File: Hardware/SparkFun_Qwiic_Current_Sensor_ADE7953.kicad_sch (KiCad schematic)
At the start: 34 parts, among them IC1 ADE7953ACPZ, J1 Qwiic_RA, J2 Qwiic_RA, J3 Conn_01x06, J4 Conn_01x04, J5 3.5mm TRRS, Y1 Resonator

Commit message: Updated PCB and Schematic
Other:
- note added: "Be sure to change these shunt resistor values!"
- note removed: "Be sure to change these shunt capacitor values!"
- moved on the sheet: R4, R5

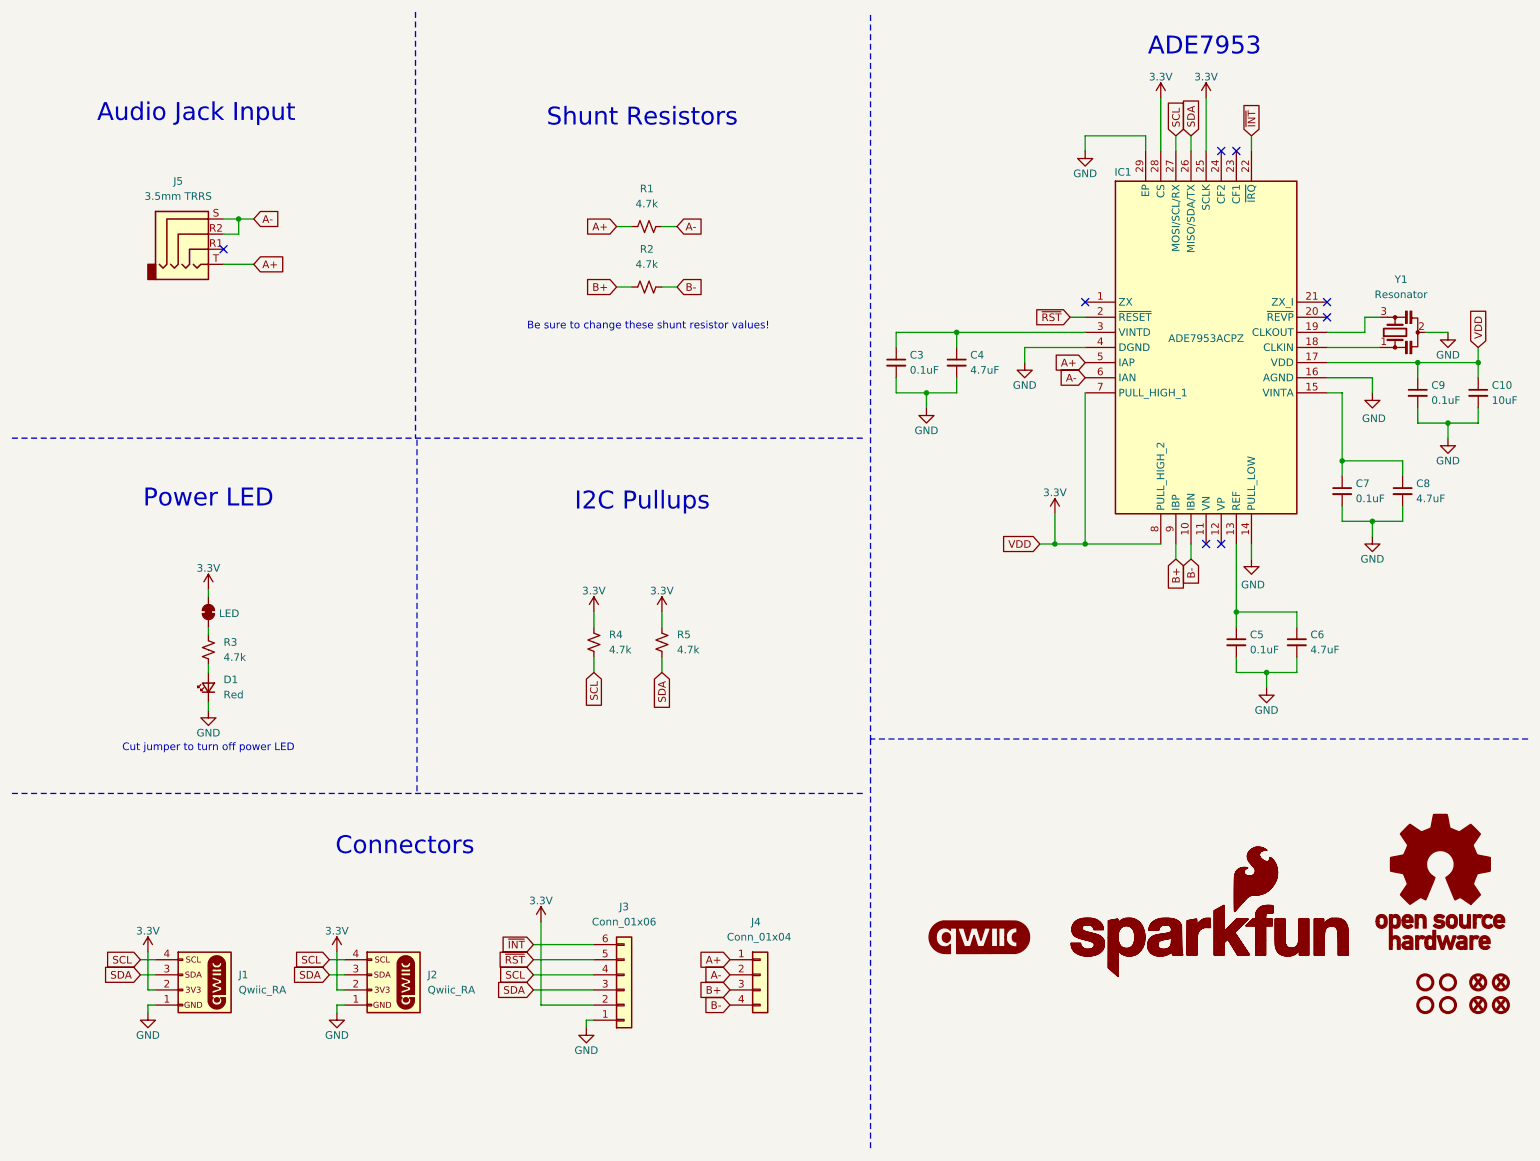
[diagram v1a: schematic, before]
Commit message: Updated IC Schematic Symbols
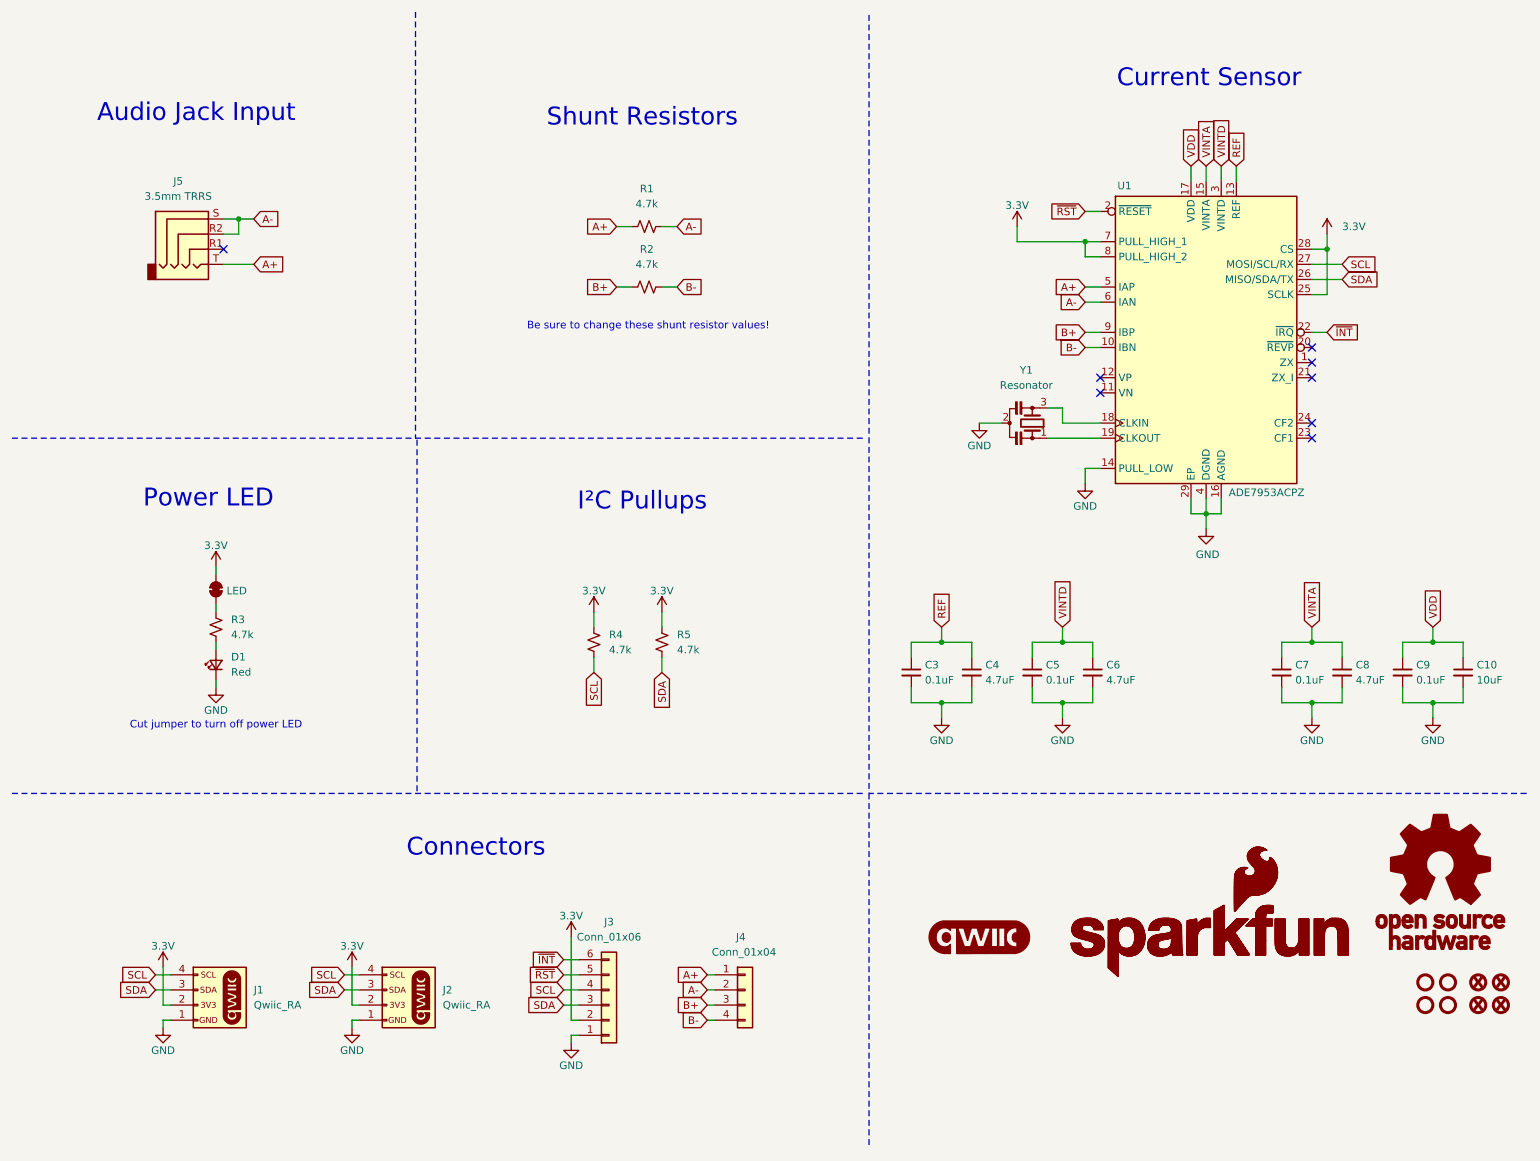
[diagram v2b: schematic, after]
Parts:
- renumbered IC1 to U1
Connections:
- net 3.3V: no longer C10.1, C9.1, U1.17 (VDD)
- net VINTD: now reaches C5.1, C6.1
- net VINTD: now also U1.3 (VINTD); no longer U1.13 (REF)
- net at Y1.1: now also U1.19 (CLKOUT); no longer U1.18 (CLKIN)
- net at Y1.3: now also U1.18 (CLKIN); no longer U1.19 (CLKOUT)
- net REF: now reaches C3.1, C4.1
- net REF: now also U1.13 (REF); no longer U1.3 (VINTD)
- net VINTA: now reaches C7.1, C8.1, U1.15 (VINTA)
- new net VDD: C10.1, C9.1, U1.17 (VDD)
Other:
- note added: "Current Sensor"
- note added: "I²C Pullups"
- note removed: "ADE7953"
- note removed: "I2C Pullups"
- title: SparkFun Qwiic 5V Boost AP3012K -> SparkFun Qwiic Current Sensor ADE7953
- moved on the sheet: C10, C3, C4, C5, C6, C7, C8, C9, D1, J1, J2, J3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

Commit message: Updated PCB Layout
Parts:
- removed C10: 10uF, SparkFun-Capacitor:C_0603_1608Metric, symbol SparkFun-Capacitor:10uF_0603_10V_20%
- removed C3, C5, C7, C9: 0.1uF, SparkFun-Capacitor:C_0603_1608Metric, symbol SparkFun-Capacitor:0.1uF_0603_25V_20%
- removed C4, C6, C8: 4.7uF, SparkFun-Capacitor:C_0603_1608Metric, symbol SparkFun-Capacitor:4.7uF_0603_35V_20%
- removed J4: Conn_01x04, SparkFun-Connector:1x04_P2.54mm, symbol SparkFun-Connector:Conn_01x04_P2.54mm
- added C1, C2, C3, C4: 1.0uF, SparkFun-Capacitor:C_0402_1005Metric, symbol SparkFun-Capacitor:1.0uF_0402_16V_10%
- added J4, J6: Conn_01x02, SparkFun-Connector:1x02_P2.54mm, symbol SparkFun-Connector:Conn_01x02_P2.54mm
- added JP2: ~, SparkFun-Jumper:Jumper_3_NC-2_Trace, symbol SparkFun-Jumper:SolderJumper_3_Bridged123
- R1, R2: value 4.7k -> 100; footprint SparkFun-Resistor:R_0603_1608Metric -> SparkFun-Resistor:R_0402_1005Metric; symbol SparkFun-Resistor:4.7k_0603 -> SparkFun-Resistor:100_0402; PROD_ID RES-07857 -> RES-25568
- R4, R5: value 4.7k -> 2.2k; footprint SparkFun-Resistor:R_0603_1608Metric -> SparkFun-Resistor:R_0402_1005Metric; symbol SparkFun-Resistor:4.7k_0603 -> SparkFun-Resistor:2.2k_0402; PROD_ID RES-07857 -> RES-25566
- U1: footprint QFN50P500X500X80-29N-D -> SparkFun-Semiconductor-Standard:QFN-28-1EP_4x4mm_P0.4mm_EP2.6x2.6mm
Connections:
- net VDD is gone; now on net 3.3V: U1.17 (VDD)
- net 3.3V: now also C4.1, JP2.2 (B); no longer R4.2, R5.2
- net A+: now also J4.1 (Pin_1)
- net A-: now also J4.2 (Pin_2)
- net B+: now also J6.1 (Pin_1)
- net B-: now also J6.2 (Pin_2)
- net GND: now also C1.2, C2.2, C3.2, C4.2
- net REF: now also C1.1
- net VINTA: now also C3.1
- net VINTD: now also C2.1
- new net: JP2.1 (A), R5.2
- new net: JP2.3 (C), R4.2
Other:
- note added: "IIC ADDR"
- note added: "SPI Settings Table"
- moved on the sheet: R5

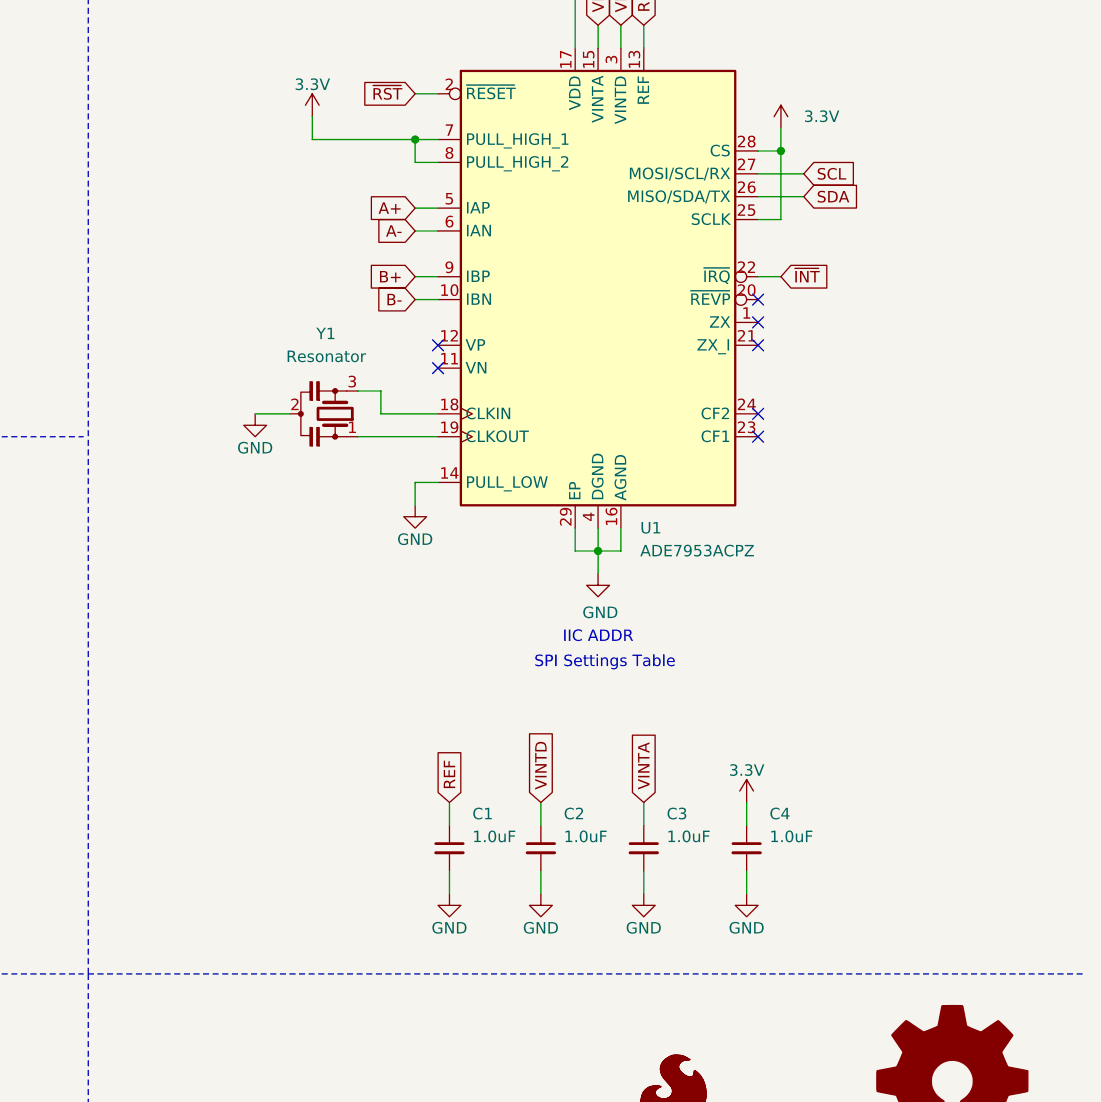
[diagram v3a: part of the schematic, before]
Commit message: Added XTAL Osc.
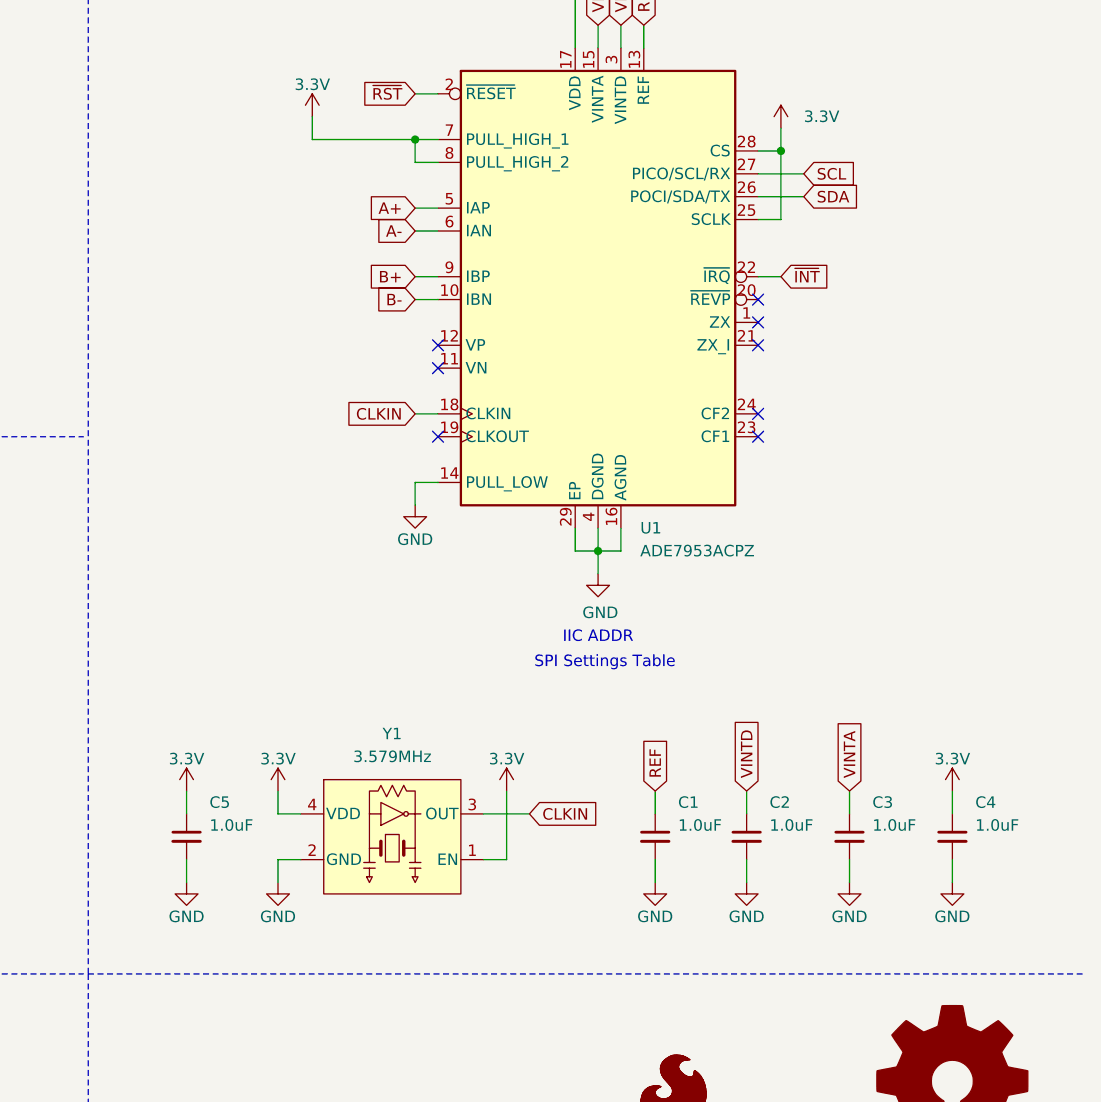
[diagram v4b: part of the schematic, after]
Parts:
- removed Y1: Resonator, symbol SparkFun-Clock:Resonator
- added C5: 1.0uF, SparkFun-Capacitor:C_0402_1005Metric, symbol SparkFun-Capacitor:1.0uF_0402_16V_10%
- added Y1: 3.579MHz, SparkFun-Clock:Crystal_SMD_3.2x2.5mm, symbol SparkFun-Clock:Oscillator_24MHz_3.2x2.5mm
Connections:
- net 3.3V: now also C5.1, Y1.1 (EN), Y1.4 (VDD)
- net GND: now also C5.2, Y1.2 (GND)
- net CLKIN: now reaches U1.18 (CLKIN)
- net CLKIN: now also Y1.3 (OUT)
- no-connect marks 8 -> 9
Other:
- moved on the sheet: C1, C2, C3, C4

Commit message: Fixed Reset Pin and Shunt Resistors
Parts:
- removed R2: 100, SparkFun-Resistor:R_0402_1005Metric, symbol SparkFun-Resistor:100_0402
- added C6, C7, C8, C9: 33pF, SparkFun-Capacitor:C_0402_1005Metric, symbol SparkFun-Capacitor:33pF_0402_50V_5%
- added R10, R7, R8, R9: 1k, SparkFun-Resistor:R_0402_1005Metric, symbol SparkFun-Resistor:1k_0402
- added R2: 5.6, SparkFun-Resistor:R_0603_1608Metric, symbol SparkFun-Resistor:5.62k_0603
- added R6: 4.7k, SparkFun-Resistor:R_0402_1005Metric, symbol SparkFun-Resistor:4.7k_0402
- R1: value 100 -> 5.6; footprint SparkFun-Resistor:R_0402_1005Metric -> SparkFun-Resistor:R_0603_1608Metric; symbol SparkFun-Resistor:100_0402 -> SparkFun-Resistor:5.62k_0603; PROD_ID RES-25568 -> RES-09823
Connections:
- net 3.3V: now also R6.2
- net A+: now also R7.1; no longer U1.5 (IAP)
- net A-: now also R8.1; no longer U1.6 (IAN)
- net B+: now also R2.2, R9.1; no longer U1.9 (IBP)
- net B-: now also R10.1, R2.1; no longer U1.10 (IBN)
- net GND: now also C6.2, C7.2, C8.2, C9.2
- net ~{RST}: now also R6.1
- new net IAN: C7.1, R8.2, U1.6 (IAN)
- new net IAP: C6.1, R7.2, U1.5 (IAP)
- new net IBN: C9.1, R10.2, U1.10 (IBN)
- new net IBP: C8.1, R9.2, U1.9 (IBP)
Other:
- note removed: "Be sure to change these shunt resistor values!"
- moved on the sheet: R1

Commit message: Implemented changes after design review
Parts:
- added JP3: SCLK, SparkFun-Jumper:Jumper_3_NC-1_Trace, symbol SparkFun-Jumper:SolderJumper_3_Bridged12
- added JP4: CS, SparkFun-Jumper:Jumper_2_NC_Trace, symbol SparkFun-Jumper:SolderJumper_2_Bridged
- added R11: 2.2k, SparkFun-Resistor:R_0402_1005Metric, symbol SparkFun-Resistor:2.2k_0402
- JP2: value ~ -> I²C
- R6: footprint SparkFun-Resistor:R_0402_1005Metric -> SparkFun-Resistor:R_0603_1608Metric; symbol SparkFun-Resistor:4.7k_0402 -> SparkFun-Resistor:4.7k_0603; PROD_ID RES-15343 -> RES-07857
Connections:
- net 3.3V: now also JP3.1 (A), JP4.2 (B); no longer U1.25 (SCLK), U1.28 (CS)
- net GND: now also R11.1
- net ZX_I: now reaches U1.21 (ZX_I)
- net ZX_I: now also J3.5 (Pin_5)
- net ~{RST}: no longer names the net of R6.1, U1.2 (~{RESET})
- net ~{RST}: no longer J3.5 (Pin_5)
- new net: JP3.2 (B), U1.25 (SCLK)
- new net: JP3.3 (C), R11.2
- new net: JP4.1 (A), U1.28 (CS)
- no-connect marks 9 -> 8
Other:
- note added: "Current Sensor - ADE7953ACPZ"
- note added: "Default 7-bit I²C Address: 0x38"
- note added: "Gain Table"
- note added: "TRRS Audio Jack Input"
- note removed: "Audio Jack Input"
- note removed: "Current Sensor"
- note removed: "IIC ADDR"
- moved on the sheet: C6, C7, C8, C9, R1, R10, R2, R6, R7, R8, R9

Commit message: Updated part libraries
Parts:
- R1, R2: symbol SparkFun-Resistor:5.62k_0603 -> SparkFun-Resistor:5.6_0603_0.1%; PROD_ID RES-09823 -> RES-28570
- U1: PROD_ID (none) -> IC-28571
- Y1: value 3.579MHz -> 3.579545MHz; symbol SparkFun-Clock:Oscillator_24MHz_3.2x2.5mm -> SparkFun-Clock:Oscillator_3.579MHz_3.2x2.5mm; PROD_ID XTAL-25500 -> XTAL-28569
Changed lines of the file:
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@@
 	)
 	(symbol
-		(lib_id "SparkFun-Clock:Oscillator_24MHz_3.2x2.5mm")
+		(lib_id "SparkFun-Clock:Oscillator_3.579MHz_3.2x2.5mm")
 		(at 190.5 128.27 0)
 		(unit 1)
@@
 			)
 		)
-		(property "Value" "3.579MHz"
+		(property "Value" "3.579545MHz"
 			(at 190.5 119.38 0)
 			(effects
@@
 			)
 		)
-		(property "Datasheet" "https://abracon.com/datasheets/ASEDV.pdf"
+		(property "Datasheet" "https://mm.digikey.com/Volume0/opasdata/d220001/medias/docus/8913/SG-210STF_X1G0041710031_en.pdf"
 			(at 190.5 138.43 0)
 			(effects
@@
 			)
 		)
-		(property "PROD_ID" "XTAL-25500"
+		(property "PROD_ID" "XTAL-28569"
 			(at 190.5 143.51 0)
 			(effects
@@
 			)
 		)
+		(property "PROD_ID" "IC-28571"
+			(at 213.36 68.58 0)
+			(effects
+				(font
+					(size 1.27 1.27)
+				)
+				(hide yes)
+			)
+		)
 		(pin "27"
 		)
@@
 	)
 	(symbol
-		(lib_id "SparkFun-Resistor:5.62k_0603")
+		(lib_id "SparkFun-Resistor:5.6_0603_0.1%")
 		(at 120.65 36.83 90)
 		(unit 1)
@@
 		)
 		(property "Value" "5.6"
-			(at 124.206 37.592 90)
+			(at 123.952 37.592 90)
 			(effects
 				(font
@@
 			)
 		)
-		(property "PROD_ID" "RES-09823"
+		(property "PROD_ID" "RES-28570"
 			(at 127.254 36.83 0)
 			(effects
@@
 	)
 	(symbol
-		(lib_id "SparkFun-Resistor:5.62k_0603")
+		(lib_id "SparkFun-Resistor:5.6_0603_0.1%")
 		(at 93.98 58.42 90)
 		(unit 1)
@@
 			)
 		)
-		(property "PROD_ID" "RES-09823"
+		(property "PROD_ID" "RES-28570"
 			(at 100.584 58.42 0)
 			(effects

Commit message: Changed 4x4 chip size to 5x5mm
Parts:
- U1: footprint SparkFun-Semiconductor-Standard:QFN-28-1EP_4x4mm_P0.4mm_EP2.6x2.6mm -> SparkFun-Semiconductor-Standard:QFN-28-1EP_4x4_5mmx5mm
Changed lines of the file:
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@@
 			)
 		)
-		(property "Footprint" "SparkFun-Semiconductor-Standard:QFN-28-1EP_4x4mm_P0.4mm_EP2.6x2.6mm"
+		(property "Footprint" "SparkFun-Semiconductor-Standard:QFN-28-1EP_4x4_5mmx5mm"
 			(at 250.19 145.72 0)
 			(effects
